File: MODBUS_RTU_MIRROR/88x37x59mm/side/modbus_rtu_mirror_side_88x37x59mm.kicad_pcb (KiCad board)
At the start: 2 copper layers, 52 x 40 mm, 38 parts, among them J1 Conn_01x04_Male, J2 Conn_01x04_Male, J3 Conn_01x06_Male, SW1 SW_Push, U1 ESP32-WROOM-32, U2 TXS0108EPW, U3 AMS1117-3.3, U4 DS3231MZ, U5 FM24C64C

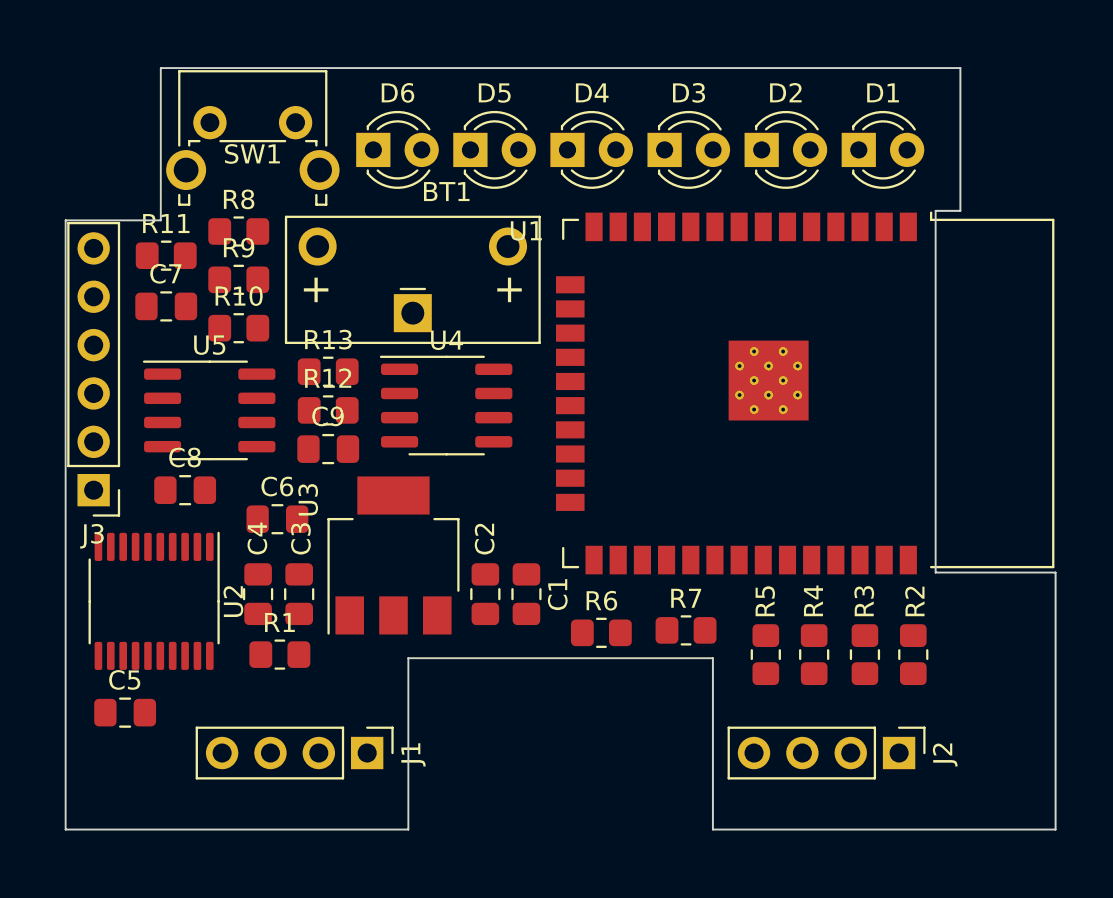
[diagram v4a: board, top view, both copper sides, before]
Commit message: all traces routed
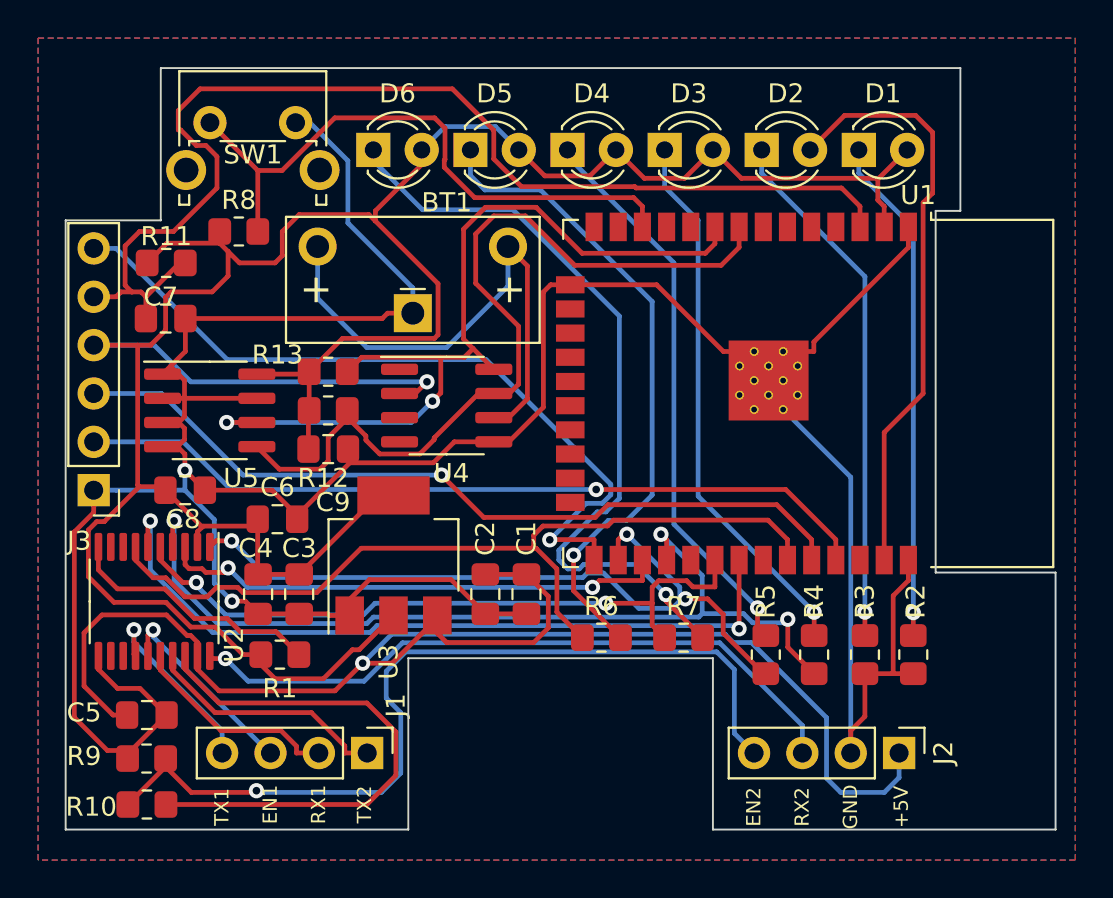
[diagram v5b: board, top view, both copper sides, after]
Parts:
- moved R9 25.6 mm to (104.3, 136.3), turned to 180 degrees
- moved R10 25.5 mm to (104.3, 138.7)
- moved C5 1.15 mm to (104.3, 134.0)
- moved C7 0.64 mm to (105.3, 113.2)
- moved R7 0.40 mm to (132.5, 129.9)
- moved R11 0.38 mm to (105.3, 110.2)
- moved R6 0.25 mm to (128.1, 129.9)
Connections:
- R10 pad 1: Net-(R10-Pad1) -> Net-(J2-Pad4)
- R9 pad 1: Net-(R10-Pad1) -> Net-(J2-Pad4)
- U1 pad 27: Net-(R10-Pad2) -> Net-(U1-Pad27)
- U2 pad 18: Net-(J2-Pad4) -> Net-(R10-Pad2)
- U2 pad 3: Net-(R10-Pad1) -> Net-(U1-Pad27)
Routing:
- net GND: track 0.00 -> 195.2 mm, vias 0 -> 2
- net +3.3V: track 0.00 -> 159.0 mm, vias 0 -> 1
- net +5V: track 0.00 -> 77.3 mm, vias 0 -> 1
- net /ESP_EN: track 0.00 -> 61.7 mm
- net /TX2_LED: track 0.00 -> 48.2 mm, vias 0 -> 3
- net /I2C0_SCL: track 0.00 -> 46.2 mm, vias 0 -> 2
- net Net-(J2-Pad4): track 0.00 -> 46.2 mm, vias 0 -> 1
- net /TX1_LED: track 0.00 -> 45.5 mm
- net /I2C0_SDA: track 0.00 -> 44.6 mm
- net /ESP_RXD: track 0.00 -> 42.5 mm, vias 0 -> 1
- net /ESP_TXD: track 0.00 -> 42.2 mm, vias 0 -> 1
- net Net-(D6-Pad1): track 0.00 -> 40.9 mm, vias 0 -> 1
- net /ESP_IO0: track 0.00 -> 40.4 mm, vias 0 -> 1
- net Net-(U1-Pad31): track 0.00 -> 40.1 mm, vias 0 -> 2
- net /RX2_LED: track 0.00 -> 39.7 mm, vias 0 -> 3
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- added copper zone on B.Cu, net GND
- added copper zone on F.Cu, net GND
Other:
- board text added: "+3.3V"
- board text added: "+5V"
- board text added: "EN"
- board text added: "EN1"
- board text added: "EN2"
- board text added: "GND"
- board text added: "IO0"
- board text added: "RX1"
- board text added: "RX2"
- board text added: "RXD"
- board text added: "TX1"
- board text added: "TX2"
- board text added: "TXD"

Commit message: silk minor updates
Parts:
- added REF**: OSHW-Symbol_6.7x6mm_SilkScreen, Symbol:OSHW-Symbol_6.7x6mm_SilkScreen, B.Cu at (148.6, 136.3)
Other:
- board text added: "MODBUS RTU MIRROR SIDE BOARD"
- board text added: "RX2 ONLY INPUT R9 = CLOSE R10 = OPEN"
- board text added: "TX2/RX2 HALF DUP R9 = OPEN R10 = CLOSE"
